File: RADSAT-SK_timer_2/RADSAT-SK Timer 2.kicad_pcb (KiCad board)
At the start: 2 copper layers, 90.2 x 95.9 mm, 70 parts, among them J201 Conn_01x07, J202 Conn_01x05_Female, J203 Conn_01x03, J204 Conn_01x02, J205 Conn_01x02, J206 Conn_01x02, J207 Conn_02x26_Odd_Even, J208 Conn_02x26_Odd_Even, Q204 IRLML2060, Q205 IRLML2060, Q206 IRLML2060, SW201 SW_Push, SW202 SW_Push, SW203 SW_Push, SW204 SW_Push, SW205 SW_Push, SW206 SW_Push, U101 LT1521, U102 Galaxia_Timer, U202 TPS3700DDCR, U230 CPC1114N, U240 CPC1114N, U250 CPC1114N, U260 CPC1114N

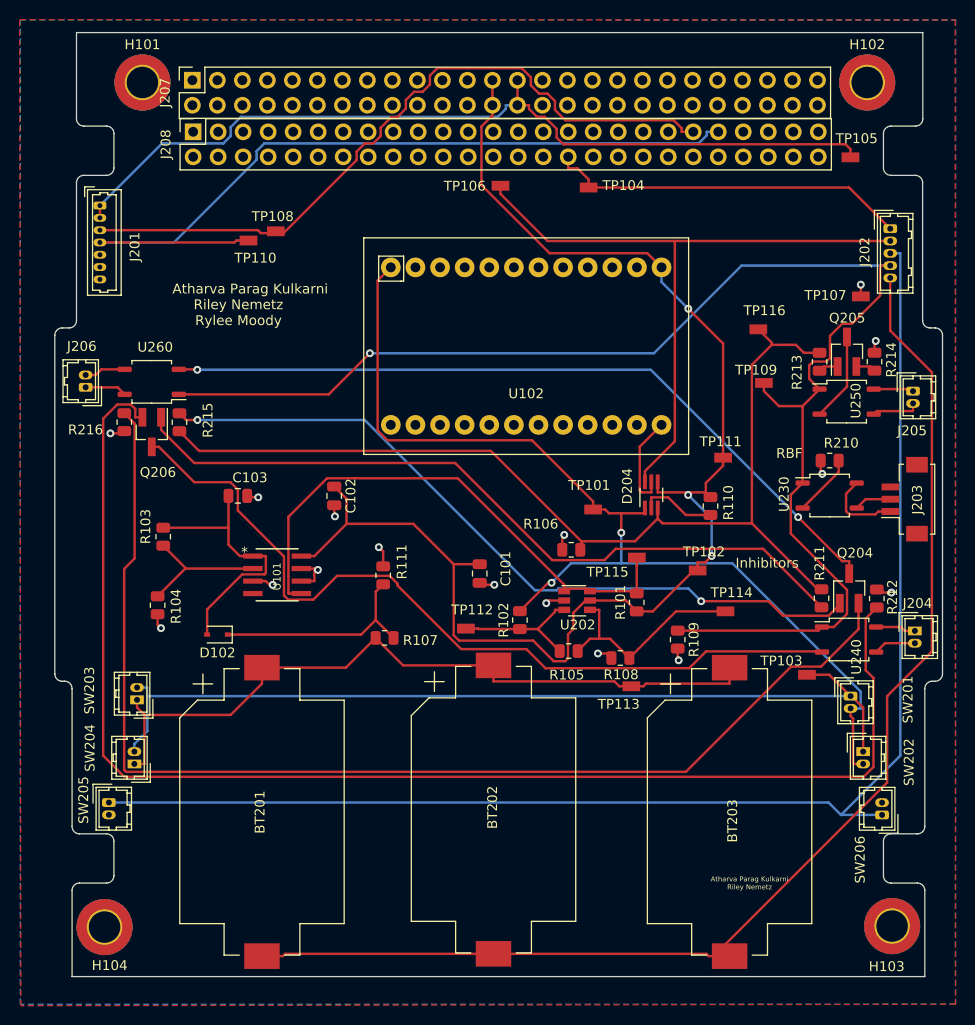
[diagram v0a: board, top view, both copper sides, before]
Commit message: places resistor above FET and rerouted PCB
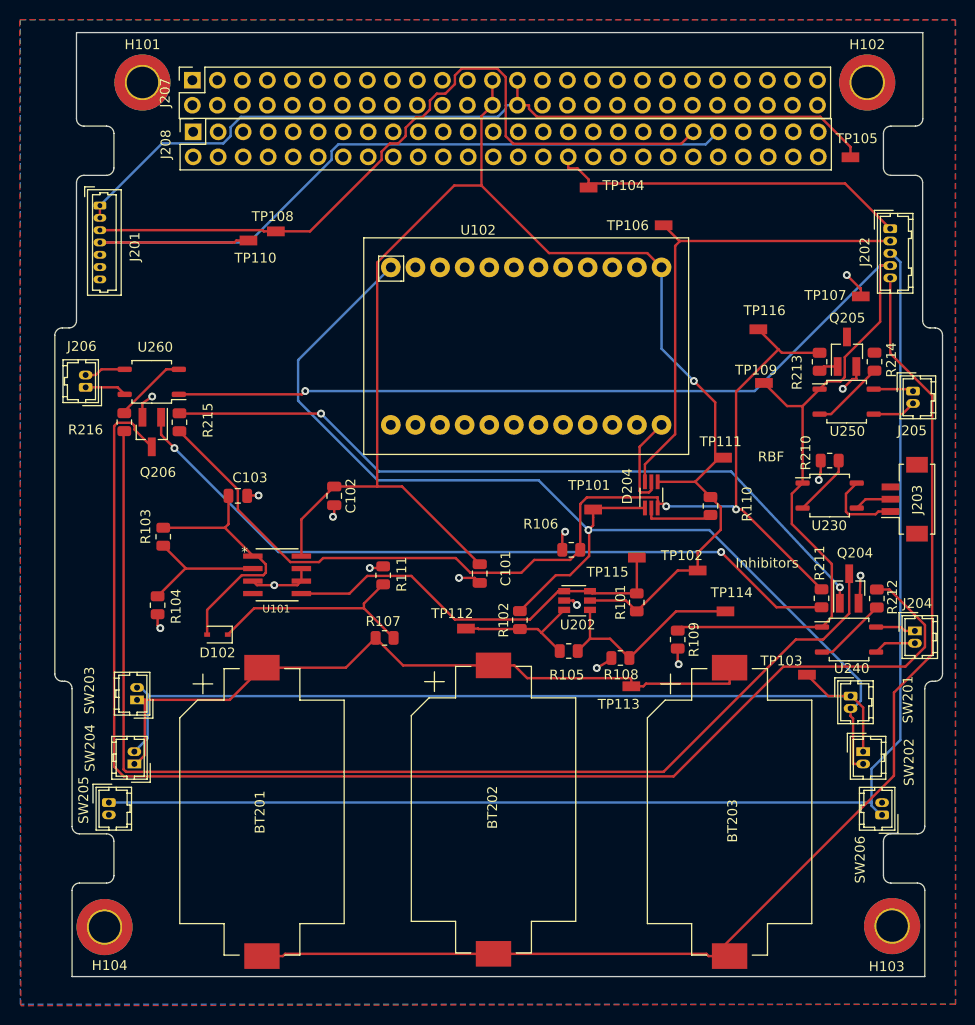
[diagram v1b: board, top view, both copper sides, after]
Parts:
- moved TP106 17.0 mm to (96.7, 69.6)
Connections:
- Q204 pad 2: Net-(Q204-Pad2) -> GND
- Q205 pad 2: Net-(Q205-Pad2) -> GND
- Q205 pad 3: Net-(Q205-Pad3) -> (no net)
- Q206 pad 2: Net-(Q206-Pad2) -> GND
- R212 pad 1: Net-(Q206-Pad2) -> Net-(R212-Pad1)
- R212 pad 2: GND -> Net-(Q206-Pad3)
- R214 pad 1: Net-(Q205-Pad2) -> Net-(R214-Pad1)
- R214 pad 2: GND -> (no net)
- R216 pad 1: Net-(Q204-Pad2) -> Net-(R216-Pad1)
- R216 pad 2: GND -> Net-(Q204-Pad3)
- U240 pad 2: Net-(Q206-Pad3) -> Net-(R212-Pad1)
- U250 pad 2: Net-(Q205-Pad3) -> Net-(R214-Pad1)
- U260 pad 2: Net-(Q204-Pad3) -> Net-(R216-Pad1)
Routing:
- net Net-(Q206-Pad2): track 136.4 -> 0.00 mm
- net Net-(Q204-Pad2): track 120.4 -> 0.00 mm
- net Net-(Q206-Pad3): track 83.8 -> 136.6 mm
- net Net-(Q204-Pad3): track 77.4 -> 118.9 mm, vias 2 -> 0
- net Net-(D204-Pad6): track 68.1 -> 49.6 mm
- net CHRG_ON-OFF: track 55.0 -> 41.6 mm
- net B: track 105.4 -> 116.1 mm, vias 2 -> 1
- net Net-(Q205-Pad3): track 8.99 -> 0.00 mm
- net +5V: track 141.6 -> 149.6 mm, vias 3 -> 1
- net Net-(R216-Pad1): track 0.00 -> 7.49 mm
- net Net-(R212-Pad1): track 0.00 -> 7.45 mm
- net Net-(R214-Pad1): track 0.00 -> 7.41 mm
- net GND: track 27.3 -> 34.6 mm, vias 16 -> 15
- net /Inhib_in: track 102.1 -> 108.5 mm, vias 0 -> 2
- net InhibV+: track 145.8 -> 141.7 mm
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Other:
- board text removed: "Atharva Parag Kulkarni"
- board text removed: "Atharva Parag Kulkarni Riley Nemetz"
- board text removed: "Riley Nemetz Rylee Moody"

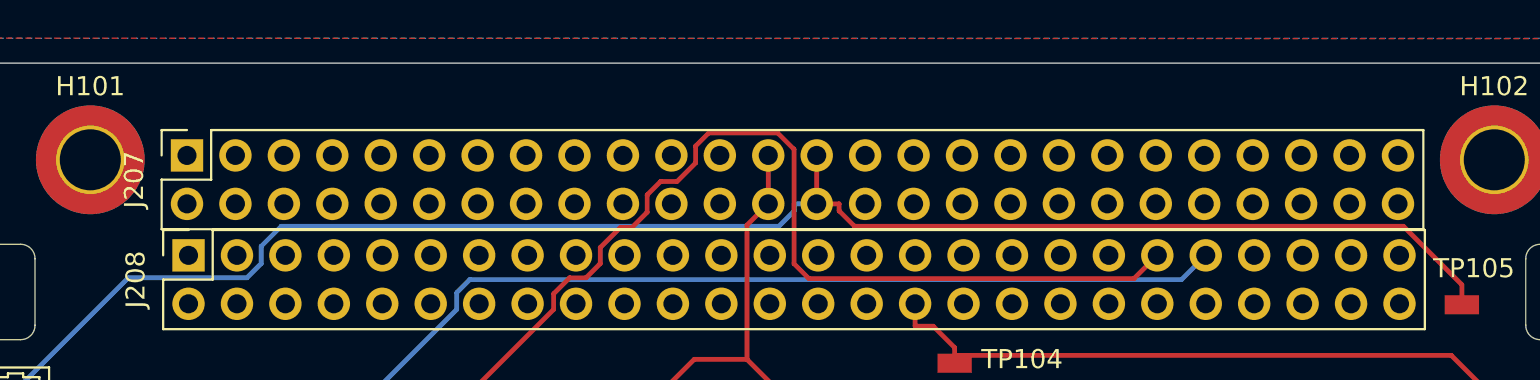
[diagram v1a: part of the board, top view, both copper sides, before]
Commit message: fixed CSKB footprint placement
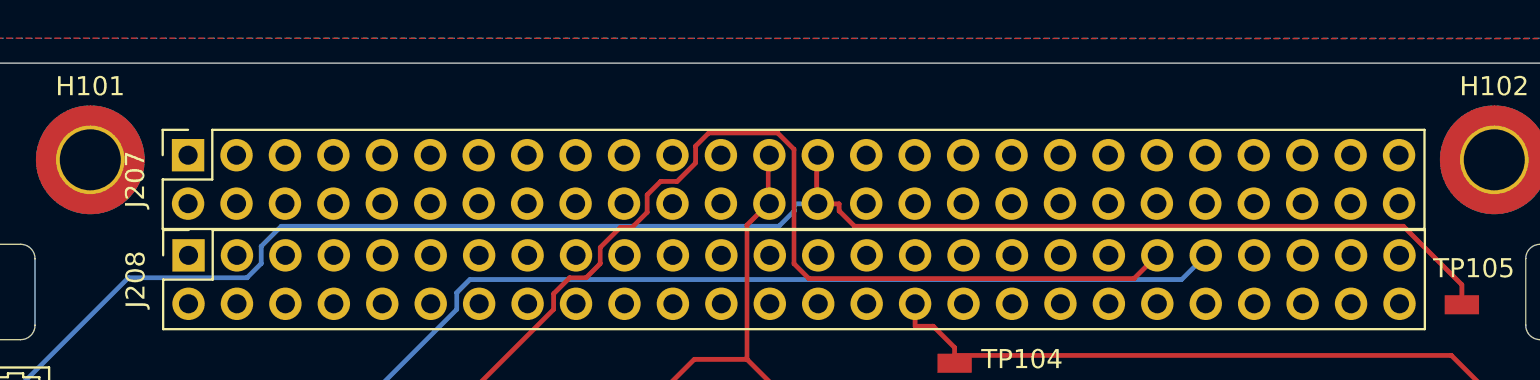
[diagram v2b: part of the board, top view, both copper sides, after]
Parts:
- moved J207 0.06 mm to (48.9, 54.8)

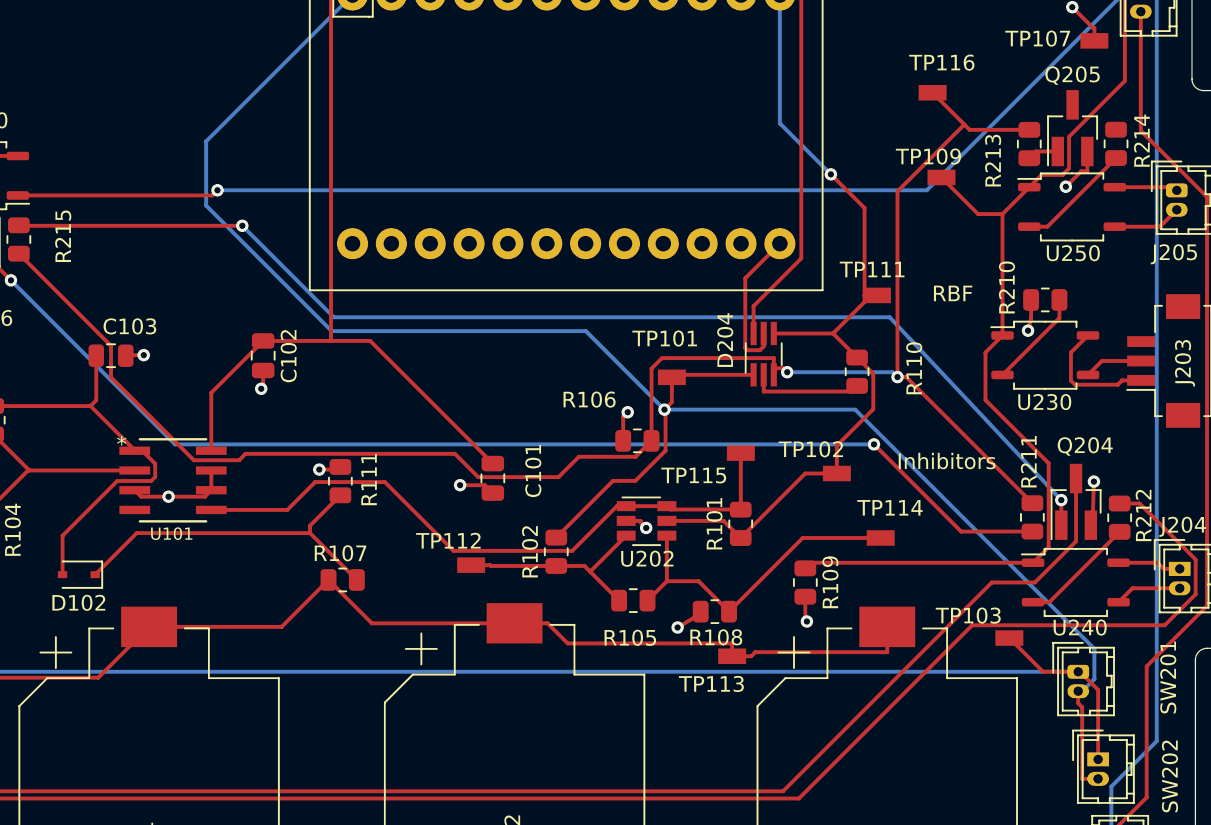
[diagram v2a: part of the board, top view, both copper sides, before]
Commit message: fixed relay connection and routed through hole resistor for current divider
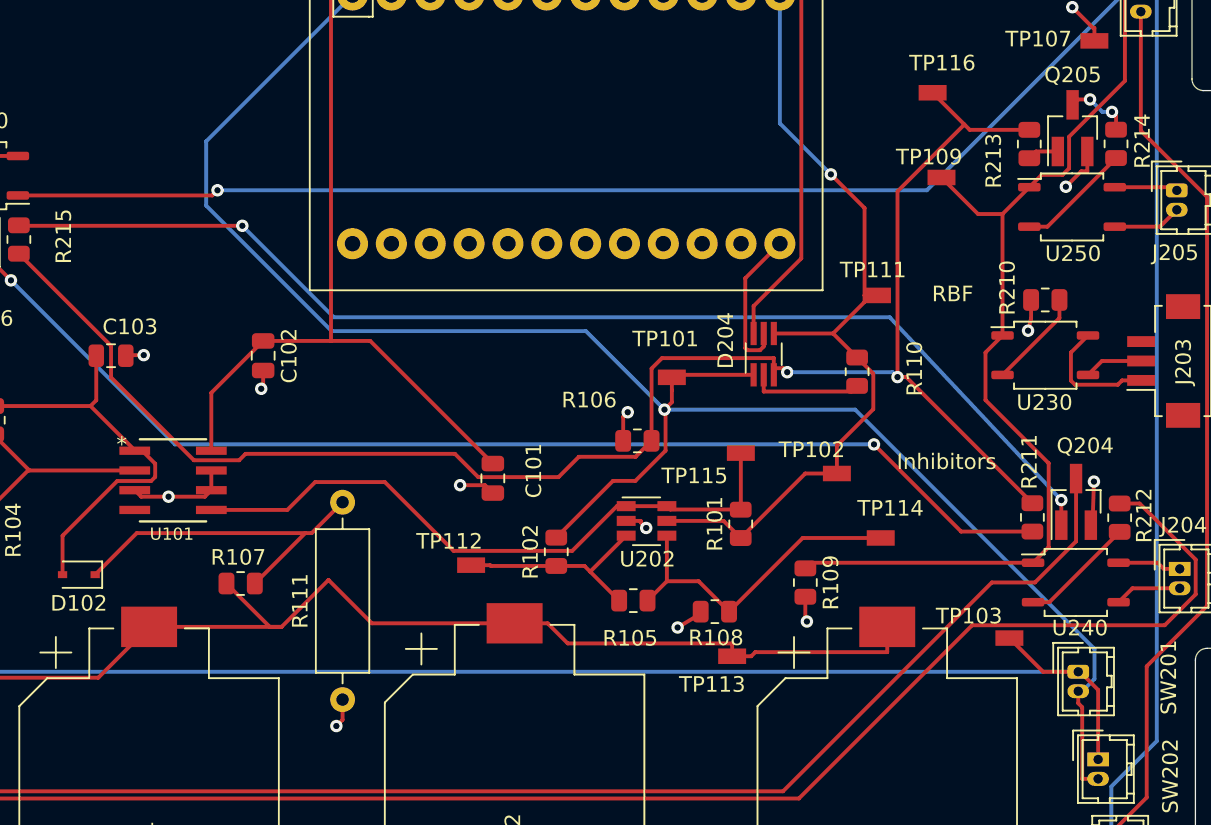
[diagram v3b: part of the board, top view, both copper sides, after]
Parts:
- R111: footprint Resistor_SMD:R_0805_2012Metric -> Resistor_THT:R_Axial_DIN0309_L9.0mm_D3.2mm_P12.70mm_Horizontal
- moved R111 14.1 mm to (68.3, 119.2), turned to 90 degrees
- moved R107 6.57 mm to (61.8, 111.7)
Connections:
- Q205 pad 3: (no net) -> Net-(Q205-Pad3)
- R214 pad 2: (no net) -> Net-(Q205-Pad3)
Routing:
- net A: track 74.1 -> 78.8 mm
- net Net-(Q205-Pad3): track 0.00 -> 4.26 mm, vias 0 -> 2

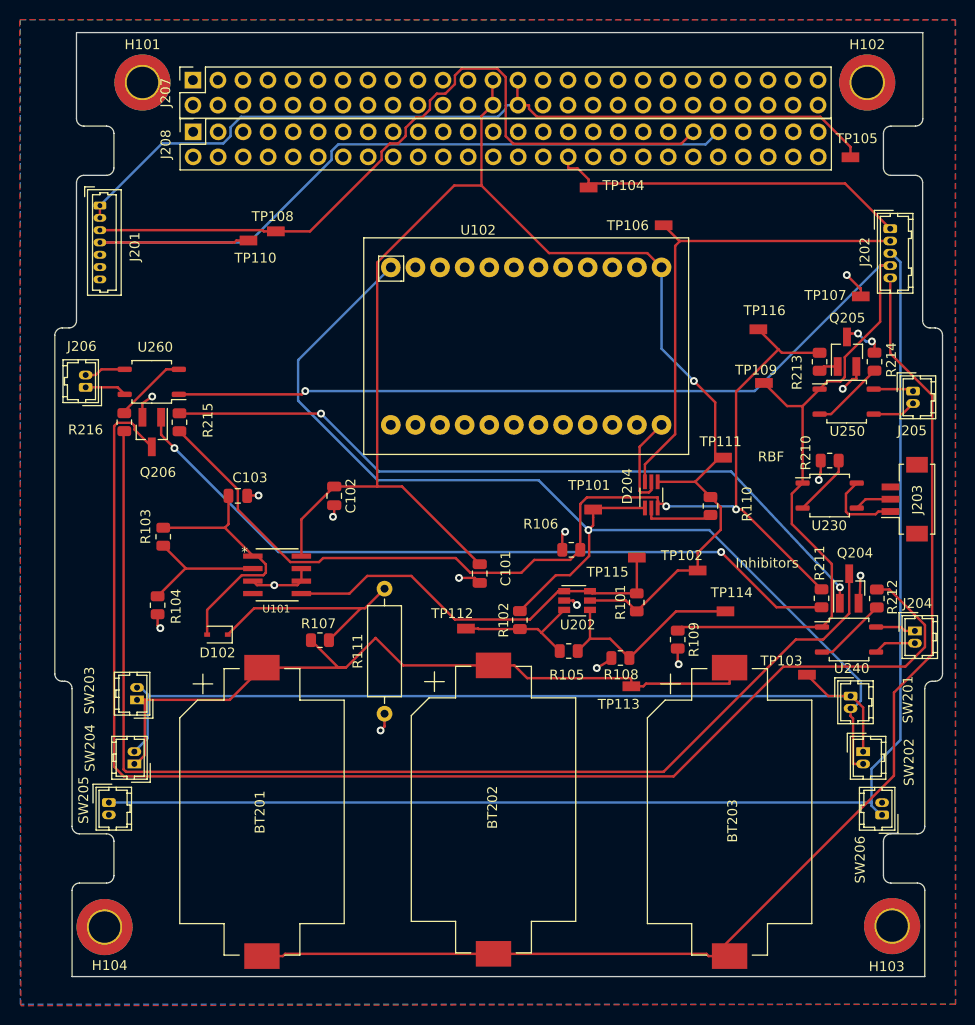
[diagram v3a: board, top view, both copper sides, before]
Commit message: PERFECTLY alligned the CSKB connectors
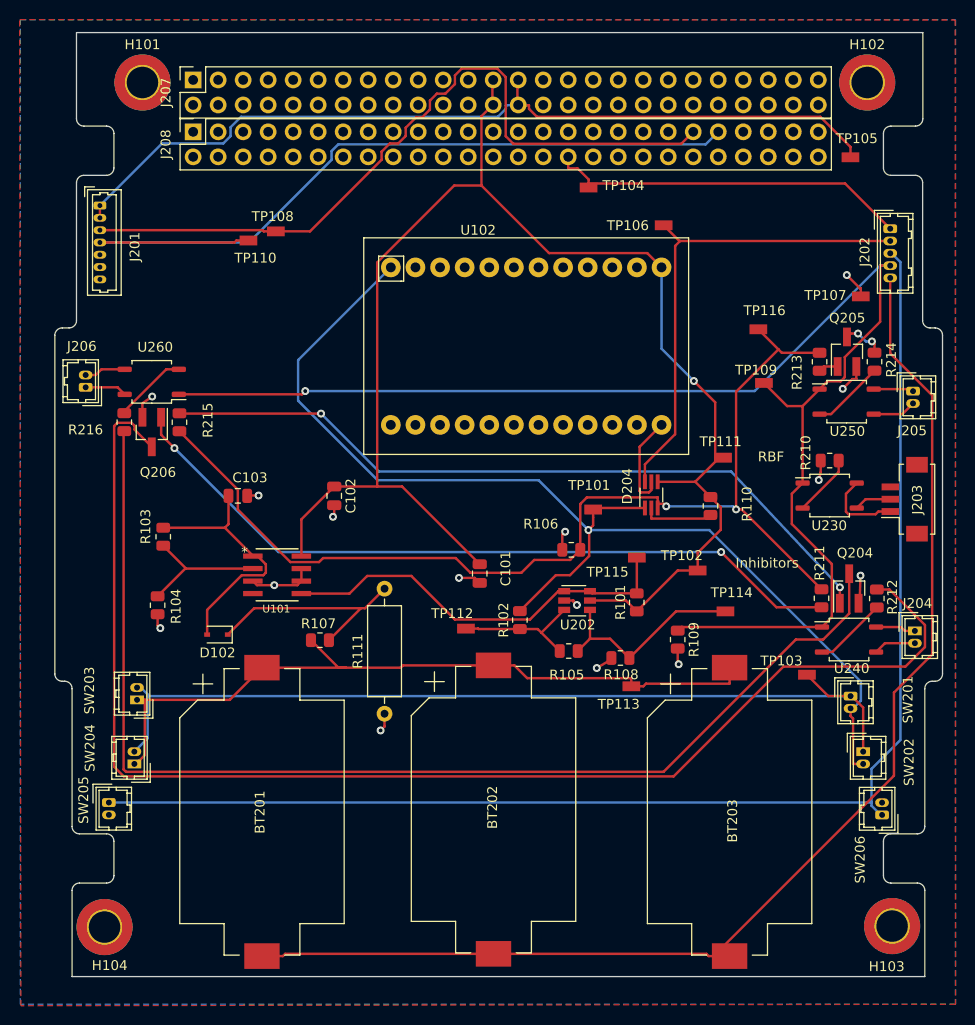
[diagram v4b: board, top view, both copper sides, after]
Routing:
- net A: track 78.8 -> 76.5 mm
